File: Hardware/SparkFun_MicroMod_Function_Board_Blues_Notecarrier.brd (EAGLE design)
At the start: 37.5 x 65 mm, 95 parts, among them J2 MICROMOD_FUNCTION_STANDARD, J6 NOTECARD, Q1 220mA/50V/3.5Ω, Q2 20V/4.2A/52mΩ/1.4W, Q3 220mA/50V/3.5Ω, Q4 20V/4.2A/52mΩ/1.4W, Q5 220mA/50V/3.5Ω, Q6 20V/4.2A/52mΩ/1.4W, U1 EEPROM, U2 TCR2EF33

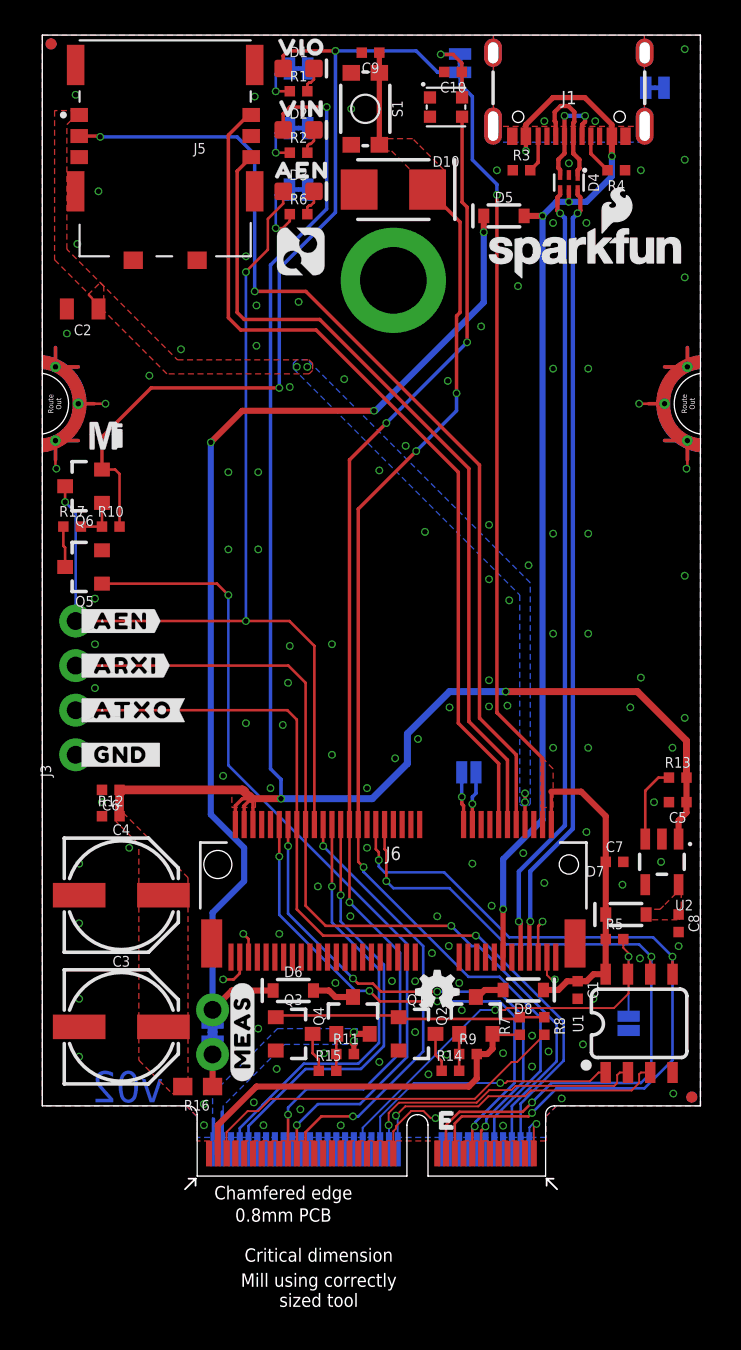
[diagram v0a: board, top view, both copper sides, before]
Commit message: Swap Notecard RX/TX, add missing silk, add diode PROD-ID.
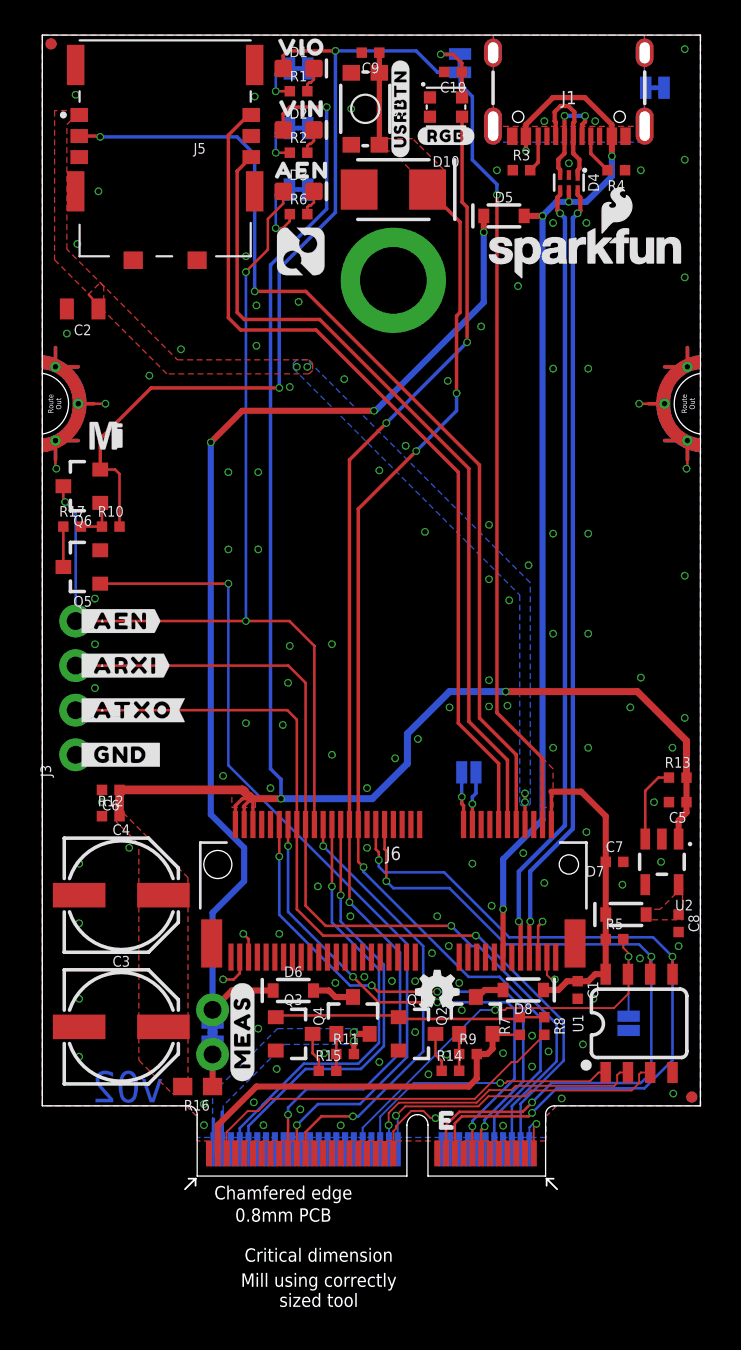
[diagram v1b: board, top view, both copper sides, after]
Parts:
- added U$25: (no value), output:#USRBTN#0
- added U$26: (no value), output:#RGB#0
- moved Q5 0.10 mm to (2.30, 34.7)
- moved Q6 0.10 mm to (2.30, 39.3)
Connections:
- net NOTECARD_RX: now also J2.15; no longer J2.13
- net NOTECARD_TX: now also J2.13; no longer J2.15
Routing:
- net NOTECARD_TX: track 29.8 -> 30.5 mm
- net GND: vias 127 -> 128

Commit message: Rev to v10. Update RGB Silk. Repanelize for changes.
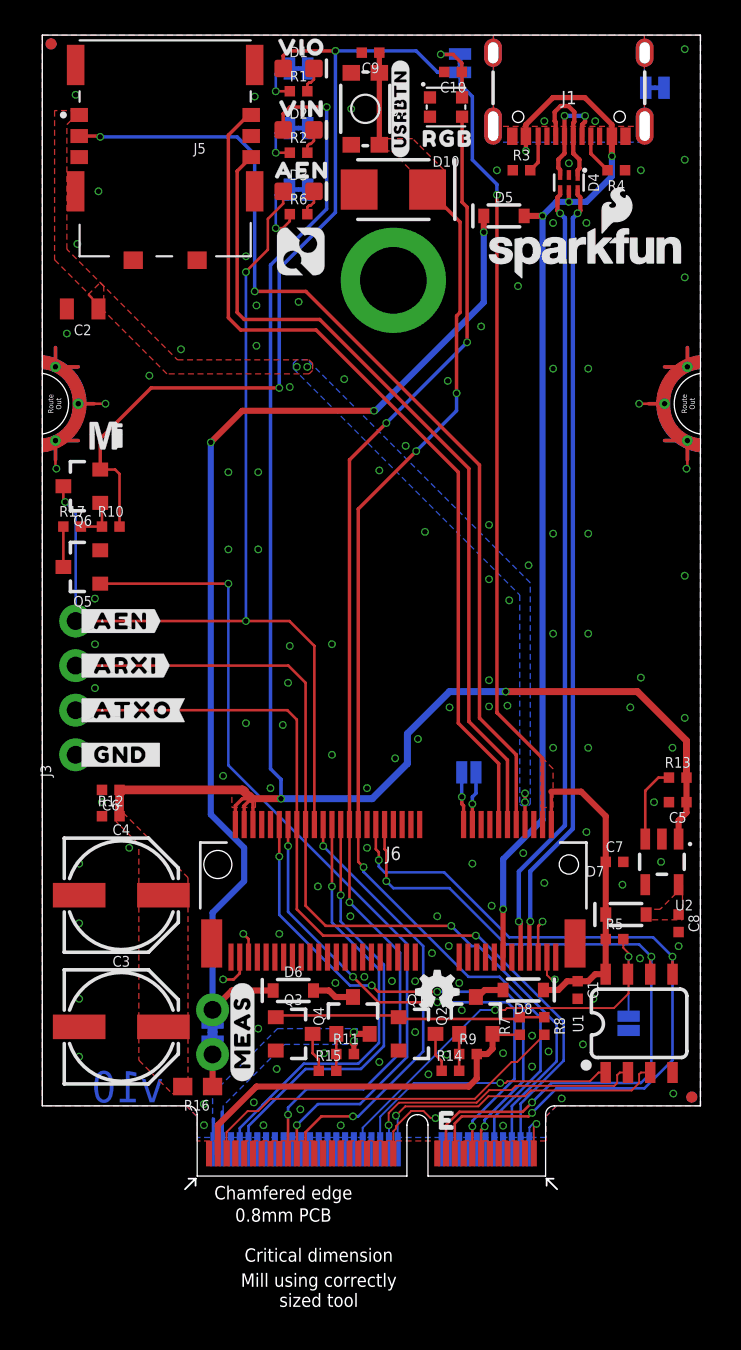
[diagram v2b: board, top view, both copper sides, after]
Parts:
- U$26: device output:#RGB#0 -> output:RGB0
- moved U$26 0.18 mm to (23.1, 59.1)
- moved U$4 0.10 mm to (22.0, 63.1)
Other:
- board text added: "v10"
- board text removed: "v02"
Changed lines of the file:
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@@
 <wire x1="29.17" y1="4" x2="37.49" y2="4" width="0" layer="20"/>
 <text x="49.2" y="-8.9" size="1.778" layer="51" font="vector">Alex Brudner</text>
-<text x="6.9" y="4.2" size="1.778" layer="16" font="vector" ratio="15" rot="MR0">v02</text>
+<text x="6.9" y="4.2" size="1.778" layer="16" font="vector" ratio="15" rot="MR0">v10</text>
 <rectangle x1="11.45" y1="12.2" x2="11.55" y2="12.7" layer="41"/>
 <rectangle x1="28.45" y1="12.3" x2="28.55" y2="12.7" layer="41"/>
@@
 <element name="U$21" library="output" package="#PWR_LED_#17" value="" x="22.4" y="59.7" smashed="yes" rot="MR0"/>
 <element name="U$19" library="output" package="#AUX_EN_LED_#20" value="" x="24.8" y="56.2" smashed="yes" rot="MR0"/>
-<element name="U$4" library="output" package="#VIO_LED_#21" value="" x="21.9" y="63.1" smashed="yes" rot="MR0"/>
+<element name="U$4" library="output" package="#VIO_LED_#21" value="" x="22" y="63.1" smashed="yes" rot="MR0"/>
 <element name="U$20" library="output" package="#_SHLD#23" value="" x="34" y="62" smashed="yes" rot="MR0"/>
 <element name="U$22" library="output" package="#_GND_#24" value="" x="7" y="24" smashed="yes" rot="MR0"/>
@@
 <element name="U$24" library="output" package="#RGB_#0" value="" x="23.8" y="59" smashed="yes" rot="MR90"/>
 <element name="U$25" library="output" package="#USRBTN#0" value="" x="20.4" y="60.8" smashed="yes" rot="R90"/>
-<element name="U$26" library="output" package="#RGB#0" value="" x="23" y="59.25" smashed="yes"/>
+<element name="U$26" library="output" package="RGB0" value="" x="23.1" y="59.1" smashed="yes"/>
 </elements>
 <signals>

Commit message: Rev v11
AEN wasn't enabled by default because it was missing a passive. Added passive and rerouted.
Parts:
- removed Q5: 220mA/50V/3.5Ω, SparkFun-DiscreteSemi:SOT23-3
- removed R17: 100, SparkFun-Resistors:0402-TIGHT
- moved R10 0.92 mm to (3.30, 36.3), turned to 90 degrees
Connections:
- removed net AUX_PWR: J2.55, Q5.1
- removed net N$19: Q6.1, R10.1, R17.2
- removed net N$20: Q5.3, R17.1
- new net !AUX_PWR!: J2.55, Q6.1, R10.2
- net 3.3V: no longer R10.2
- net GND: now also R10.1; no longer Q5.2
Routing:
- net !AUX_PWR!: track 0.00 -> 52.3 mm, vias 0 -> 2
- net AUX_PWR: track 48.0 -> 0.00 mm, vias 2 -> 0
- net 3.3V: track 112.6 -> 108.4 mm
- net N$19: track 2.59 -> 0.00 mm
- net N$20: track 2.30 -> 0.00 mm
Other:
- board text added: "v11"
- board text removed: "v10"
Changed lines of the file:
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@@
 <drawing>
 <settings>
-<setting alwaysvectorfont="yes"/>
+<setting alwaysvectorfont="no"/>
 <setting verticaltext="up"/>
 </settings>
@@
 <wire x1="29.17" y1="4" x2="37.49" y2="4" width="0" layer="20"/>
 <text x="49.2" y="-8.9" size="1.778" layer="51" font="vector">Alex Brudner</text>
-<text x="6.9" y="4.2" size="1.778" layer="16" font="vector" ratio="15" rot="MR0">v10</text>
+<text x="6.9" y="4.2" size="1.778" layer="16" font="vector" ratio="15" rot="MR0">v11</text>
 <rectangle x1="11.45" y1="12.2" x2="11.55" y2="12.7" layer="41"/>
 <rectangle x1="28.45" y1="12.3" x2="28.55" y2="12.7" layer="41"/>
@@
 <attribute name="VALUE" x="24.943" y="63.4" size="0.6096" layer="28" font="vector" ratio="20" rot="MR270" align="top-center"/>
 </element>
-<element name="Q5" library="SparkFun-DiscreteSemi" package="SOT23-3" value="220mA/50V/3.5Ω" x="2.3" y="34.7" smashed="yes" rot="R90">
-<attribute name="NAME" x="2.3" y="33.049" size="0.6096" layer="25" font="vector" ratio="20" rot="R180" align="bottom-center"/>
-<attribute name="PROD_ID" value="TRANS-00830" x="-9.3" y="34.7" size="1.778" layer="27" font="vector" ratio="15" rot="R90" display="off"/>
-<attribute name="VALUE" x="2.3" y="36.351" size="0.6096" layer="27" font="vector" ratio="20" rot="R180" align="top-center"/>
-</element>
 <element name="Q6" library="SparkFun-DiscreteSemi" package="SOT23-3" value="20V/4.2A/52mΩ/1.4W" x="2.3" y="39.3" smashed="yes" rot="R90">
 <attribute name="NAME" x="2.3" y="37.649" size="0.6096" layer="25" font="vector" ratio="20" rot="R180" align="bottom-center"/>
 <attribute name="PROD_ID" value="TRANS-14388" x="4.9" y="39.3" size="1.778" layer="27" font="vector" ratio="15" rot="R90" display="off"/>
 <attribute name="VALUE" x="2.3" y="40.951" size="0.6096" layer="27" font="vector" ratio="20" rot="R180" align="top-center"/>
-</element>
-<element name="R10" library="SparkFun-Resistors" package="0402-TIGHT" value="10k" x="3.9" y="37" smashed="yes">
-<attribute name="NAME" x="3.9" y="37.562" size="0.6096" layer="25" font="vector" ratio="20" align="bottom-center"/>
-<attribute name="PROD_ID" value="RES-14241" x="-0.4" y="34.4" size="1.778" layer="27" font="vector" ratio="15" display="off"/>
-<attribute name="VALUE" x="3.9" y="36.438" size="0.6096" layer="27" font="vector" ratio="20" align="top-center"/>
-</element>
-<element name="R17" library="SparkFun-Resistors" package="0402-TIGHT" value="100" x="1.7" y="37" smashed="yes">
-<attribute name="NAME" x="1.7" y="37.562" size="0.6096" layer="25" font="vector" ratio="20" align="bottom-center"/>
-<attribute name="PROD_ID" value="RES-14962" x="-4.7" y="31.5" size="1.778" layer="27" font="vector" ratio="15" display="off"/>
-<attribute name="VALUE" x="1.7" y="36.438" size="0.6096" layer="27" font="vector" ratio="20" align="top-center"/>
 </element>
 <element name="U$23" library="notehub" package="NOTEHUB_BLUES#SVG5" value="" x="13.4" y="54" smashed="yes"/>
@@
 <element name="U$25" library="output" package="#USRBTN#0" value="" x="20.4" y="60.8" smashed="yes" rot="R90"/>
 <element name="U$26" library="output" package="RGB0" value="" x="23.1" y="59.1" smashed="yes"/>
+<element name="R10" library="SparkFun-Resistors" package="0402-TIGHT" value="10k" x="3.3" y="36.3" smashed="yes" rot="R90">
+<attribute name="NAME" x="2.738" y="36.3" size="0.6096" layer="25" font="vector" ratio="20" rot="R90" align="bottom-center"/>
+<attribute name="PROD_ID" value="RES-14241" x="3.3" y="37" size="1.778" layer="27" rot="R90" display="off"/>
+<attribute name="VALUE" x="3.862" y="36.3" size="0.6096" layer="27" font="vector" ratio="20" rot="R90" align="top-center"/>
+</element>
 </elements>
 <signals>
@@
 <contactref element="C10" pad="2"/>
 <contactref element="D10" pad="GND"/>
-<contactref element="Q5" pad="2"/>
 <via x="25" y="48.4" extent="1-16" drill="0.3"/>
 <via x="27.1" y="50.7" extent="1-16" drill="0.3"/>
@@
 <via x="36.6" y="64.2" extent="1-16" drill="0.3"/>
 <via x="18.35" y="11.35" extent="1-16" drill="0.3"/>
+<contactref element="R10" pad="1"/>
 </signal>
 <signal name="3.3V" class="3">
@@
 <wire x1="25.9" y1="26.4" x2="28.5" y2="23.8" width="0.2" layer="1"/>
 <contactref element="RGB" pad="2"/>
-<contactref element="R10" pad="2"/>
 <contactref element="Q6" pad="2"/>
 <via x="25.9" y="55.9" extent="1-16" drill="0.3"/>
@@
 <wire x1="13.723" y1="63.823" x2="14" y2="64.1" width="0.2" layer="1"/>
 <wire x1="21.3" y1="64.1" x2="22.5207" y2="62.8793" width="0.2" layer="16"/>
-<wire x1="3.3" y1="40.25" x2="4.15" y2="40.25" width="0.15" layer="1"/>
-<wire x1="4.15" y1="40.25" x2="4.4" y2="40" width="0.15" layer="1"/>
-<wire x1="4.4" y1="40" x2="4.4" y2="37" width="0.15" layer="1"/>
 <via x="13.5" y="44.9" extent="1-16" drill="0.3"/>
 <wire x1="3.3" y1="42" x2="3.3" y2="40.25" width="0.2" layer="1"/>
@@
 <wire x1="23.915" y1="62.885" x2="23.915" y2="61.45" width="0.2" layer="1"/>
 </signal>
-<signal name="AUX_PWR">
-<contactref element="Q5" pad="1"/>
+<signal name="!AUX_PWR!">
 <contactref element="J2" pad="55"/>
 <via x="14.5" y="2.9" extent="1-16" drill="0.3"/>
@@
 <wire x1="10.6" y1="33.75" x2="10.6" y2="23.4" width="0.15" layer="16"/>
 <wire x1="10.6" y1="23.4" x2="20.78" y2="13.22" width="0.15" layer="16"/>
-<wire x1="10.6" y1="33.75" x2="3.3" y2="33.75" width="0.15" layer="1"/>
-</signal>
-<signal name="N$19">
 <contactref element="Q6" pad="1"/>
-<contactref element="R10" pad="1"/>
-<contactref element="R17" pad="2"/>
-<wire x1="2.2" y1="37" x2="3.4" y2="37" width="0.15" layer="1"/>
+<contactref element="R10" pad="2"/>
 <wire x1="3.3" y1="38.35" x2="3.4" y2="38.25" width="0.15" layer="1"/>
-<wire x1="3.4" y1="38.25" x2="3.4" y2="37" width="0.15" layer="1"/>
-</signal>
-<signal name="N$20">
-<contactref element="R17" pad="1"/>
-<contactref element="Q5" pad="3"/>
-<wire x1="1.2" y1="37" x2="1.2" y2="34.7" width="0.15" layer="1"/>
+<wire x1="3.3" y1="36.8" x2="3.3" y2="38.35" width="0.15" layer="1"/>
+<wire x1="3.3" y1="38.35" x2="7.2" y2="38.35" width="0.15" layer="1"/>
+<wire x1="10.6" y1="34.95" x2="10.6" y2="33.75" width="0.15" layer="1"/>
+<wire x1="10.6" y1="34.95" x2="7.2" y2="38.35" width="0.15" layer="1"/>
 </signal>
 </signals>

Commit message: DNP unused diode.
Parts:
- D9: value SMBJP6KE6.8A-TP -> SMBJP6KE-DNP
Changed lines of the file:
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@@
 <attribute name="VALUE" x="18.7" y="64.562" size="0.6096" layer="27" font="vector" ratio="20" rot="R180" align="top-center"/>
 </element>
-<element name="D9" library="SparkFun_MicroMod_Function_Board_Blues_Notecarrier" package="DO-214AA" value="SMBJP6KE6.8A-TP" x="20" y="56.2" smashed="yes">
-<attribute name="I_PP" value="58.1A" x="20" y="56.2" size="1.778" layer="27" font="vector" ratio="15" display="off"/>
-<attribute name="PROD_ID" value="DIO-17055" x="20" y="56.2" size="1.778" layer="27" font="vector" ratio="15" display="off"/>
-<attribute name="P_PK" value="600W" x="20" y="56.2" size="1.778" layer="27" font="vector" ratio="15" display="off"/>
-<attribute name="VCLMP" value="10.5V" x="20" y="56.2" size="1.778" layer="27" font="vector" ratio="15" display="off"/>
-<attribute name="VWM" value="5.8V" x="20" y="56.2" size="1.778" layer="27" font="vector" ratio="15" display="off"/>
+<element name="D9" library="SparkFun_MicroMod_Function_Board_Blues_Notecarrier" package="DO-214AA" value="SMBJP6KE-DNP" x="20" y="56.2" smashed="yes">
+<attribute name="PROD_ID" value="" x="20" y="56.2" size="1.778" layer="27" font="vector" ratio="15" display="off"/>
 </element>
 <element name="D10" library="SparkFun-LED" package="WS2812-2020" value="WS2812_2020" x="23" y="60.9" smashed="yes" rot="R180">
